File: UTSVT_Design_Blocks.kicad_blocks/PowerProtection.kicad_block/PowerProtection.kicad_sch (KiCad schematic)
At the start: 16 parts, among them IC1 LM74502DDFR, Q1 PSMN012-100YS, Q2 PSMN012-100YS

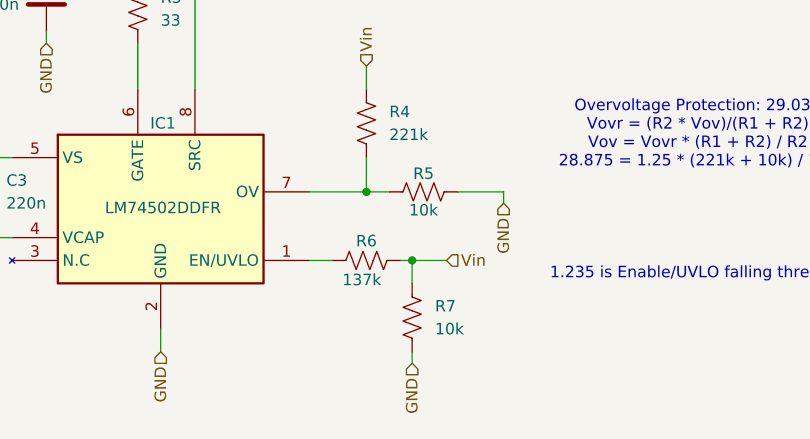
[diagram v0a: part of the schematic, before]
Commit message: fixed unvlo and made source and gate hieracrhical labels
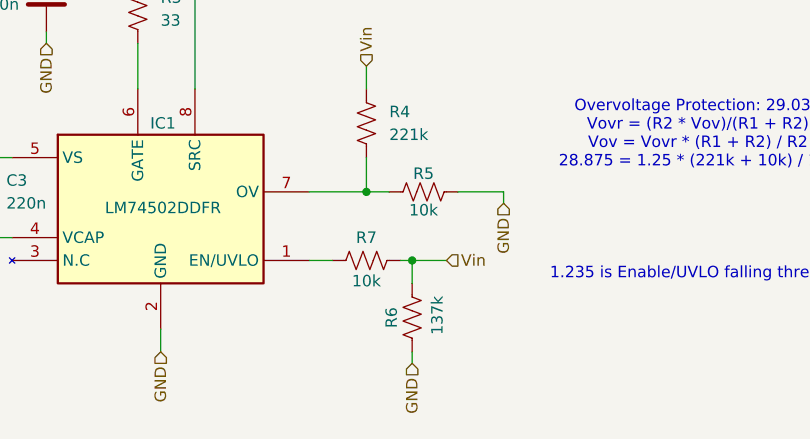
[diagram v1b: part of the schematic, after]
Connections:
- net GND: now also R6.2; no longer R7.1
- net Vin: now also R6.1; no longer R6.2
- net at IC1.1 (EN/UVLO): now also R7.1; no longer R6.1
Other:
- moved on the sheet: R6, R7
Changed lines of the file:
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@@
 	(symbol
 		(lib_id "Device:R_US")
-		(at 102.87 95.25 180)
+		(at 97.79 88.9 90)
 		(unit 1)
 		(exclude_from_sim no)
@@
 		(on_board yes)
 		(dnp no)
-		(fields_autoplaced yes)
 		(property "Reference" "R7"
-			(at 105.41 93.9799 0)
-			(effects
-				(font
-					(size 1.27 1.27)
-				)
-				(justify right)
+			(at 97.79 86.36 90)
+			(effects
+				(font
+					(size 1.27 1.27)
+				)
 			)
 		)
 		(property "Value" "10k"
-			(at 105.41 96.5199 0)
-			(effects
-				(font
-					(size 1.27 1.27)
-				)
-				(justify right)
+			(at 97.79 91.186 90)
+			(effects
+				(font
+					(size 1.27 1.27)
+				)
 			)
 		)
 		(property "Footprint" "Resistor_SMD:R_0603_1608Metric_Pad0.98x0.95mm_HandSolder"
-			(at 101.854 94.996 90)
+			(at 98.044 87.884 90)
 			(effects
 				(font
@@
 		)
 		(property "Datasheet" "~"
-			(at 102.87 95.25 0)
+			(at 97.79 88.9 0)
 			(effects
 				(font
@@
 		)
 		(property "Description" "Resistor, US symbol"
-			(at 102.87 95.25 0)
+			(at 97.79 88.9 0)
 			(effects
 				(font
@@
 		)
 		(property "P/N" "CRCW060310K0FKEI"
-			(at 102.87 95.25 0)
+			(at 97.79 88.9 0)
 			(effects
 				(font
@@
 		)
 		(property "LCSC P/N" "C25804"
-			(at 102.87 95.25 0)
+			(at 97.79 88.9 0)
 			(effects
 				(font
@@
 	(symbol
 		(lib_id "Device:R_US")
-		(at 97.79 88.9 90)
+		(at 102.87 95.25 0)
 		(unit 1)
 		(exclude_from_sim no)
@@
 		(dnp no)
 		(property "Reference" "R6"
-			(at 97.79 86.741 90)
+			(at 100.584 95.25 90)
 			(effects
 				(font
@@
 		)
 		(property "Value" "137k"
-			(at 97.282 91.059 90)
+			(at 105.664 94.996 90)
 			(effects
 				(font
@@
 		)
 		(property "Footprint" "Resistor_SMD:R_0603_1608Metric_Pad0.98x0.95mm_HandSolder"
-			(at 98.044 87.884 90)
+			(at 103.886 95.504 90)
 			(effects
 				(font
@@
 		)
 		(property "Datasheet" "~"
-			(at 97.79 88.9 0)
+			(at 102.87 95.25 0)
 			(effects
 				(font
@@
 		)
 		(property "Description" "Resistor, US symbol"
-			(at 97.79 88.9 0)
+			(at 102.87 95.25 0)
 			(effects
 				(font
@@
 		)
 		(property "P/N" "CRCW0603137KFKEA"
-			(at 97.79 88.9 90)
+			(at 102.87 95.25 90)
 			(effects
 				(font
@@
 		)
 		(property "LCSC P/N" "C2090646"
-			(at 97.79 88.9 90)
+			(at 102.87 95.25 90)
 			(effects
 				(font
@@
 		)
 		(instances
-			(project ""
+			(project "PowerProtection"
 				(path "/a968d2b9-0c0e-491c-a5a4-aacd8448ff64"
 					(reference "R6")

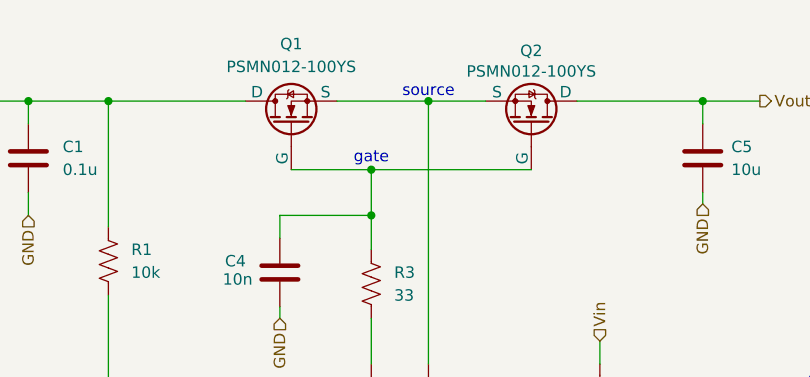
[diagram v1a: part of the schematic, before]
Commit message: fixed unvlo and made source and gate hieracrhical labels
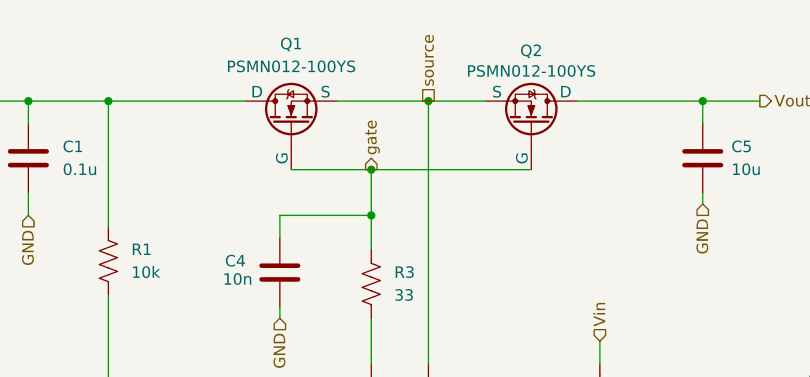
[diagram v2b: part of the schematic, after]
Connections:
- net gate: now reaches C4.1, Q1.2 (G), Q2.2 (G), R3.1
- net source: now reaches IC1.8 (SRC), Q1.3 (S), Q2.3 (S)
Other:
- note removed: "gate"
- note removed: "source"
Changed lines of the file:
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@@
-		)
-	)
-	(text "gate"
-		(exclude_from_sim no)
-		(at 72.39 46.99 0)
-		(effects
-			(font
-				(size 1.27 1.27)
-			)
 		)
 	)
@@
 		(exclude_from_sim no)
 		(at 134.62 74.93 0)
-		(effects
-			(font
-				(size 1.27 1.27)
-			)
-		)
-	)
-	(text "source"
-		(exclude_from_sim no)
-		(at 78.74 39.624 0)
 		(effects
 			(font
@@
 		)
 	)
+	(hierarchical_label "gate"
+		(shape output)
+		(at 72.39 48.26 90)
+		(effects
+			(font
+				(size 1.27 1.27)
+			)
+			(justify left)
+		)
+	)
 	(hierarchical_label "GND"
 		(shape input)
@@
 		)
 	)
+	(hierarchical_label "source"
+		(shape passive)
+		(at 78.74 40.64 90)
+		(effects
+			(font
+				(size 1.27 1.27)
+			)
+			(justify left)
+		)
+	)
